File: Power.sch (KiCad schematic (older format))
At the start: 3 parts

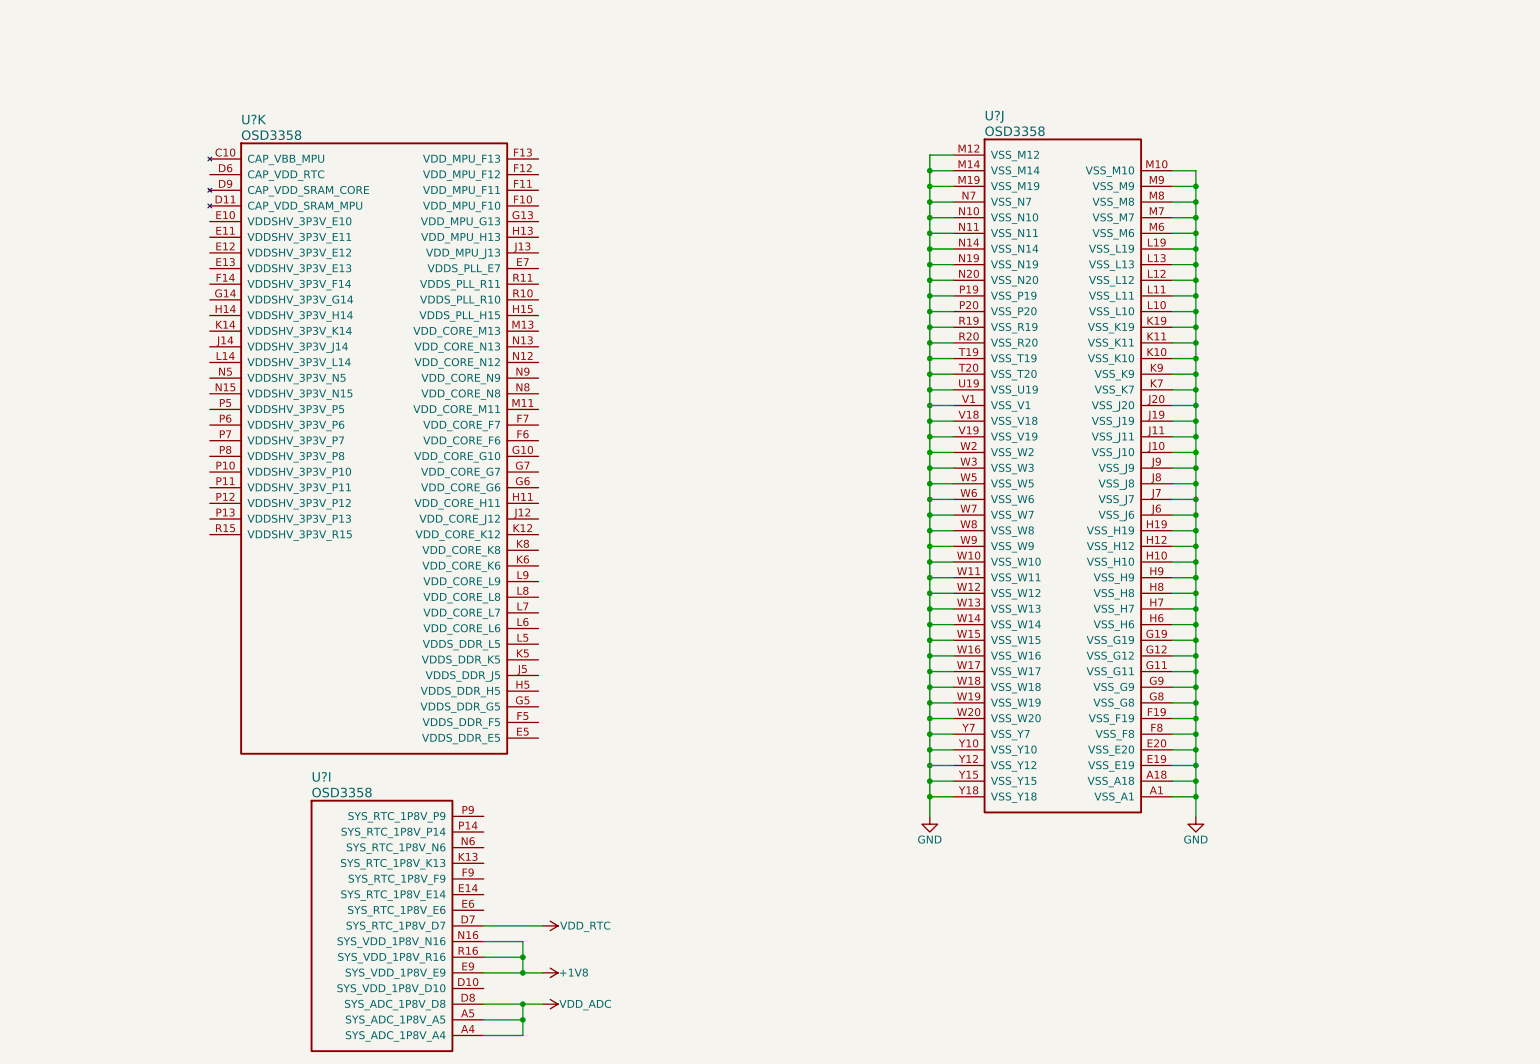
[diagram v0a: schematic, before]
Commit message: Added analog and GPIO sheet
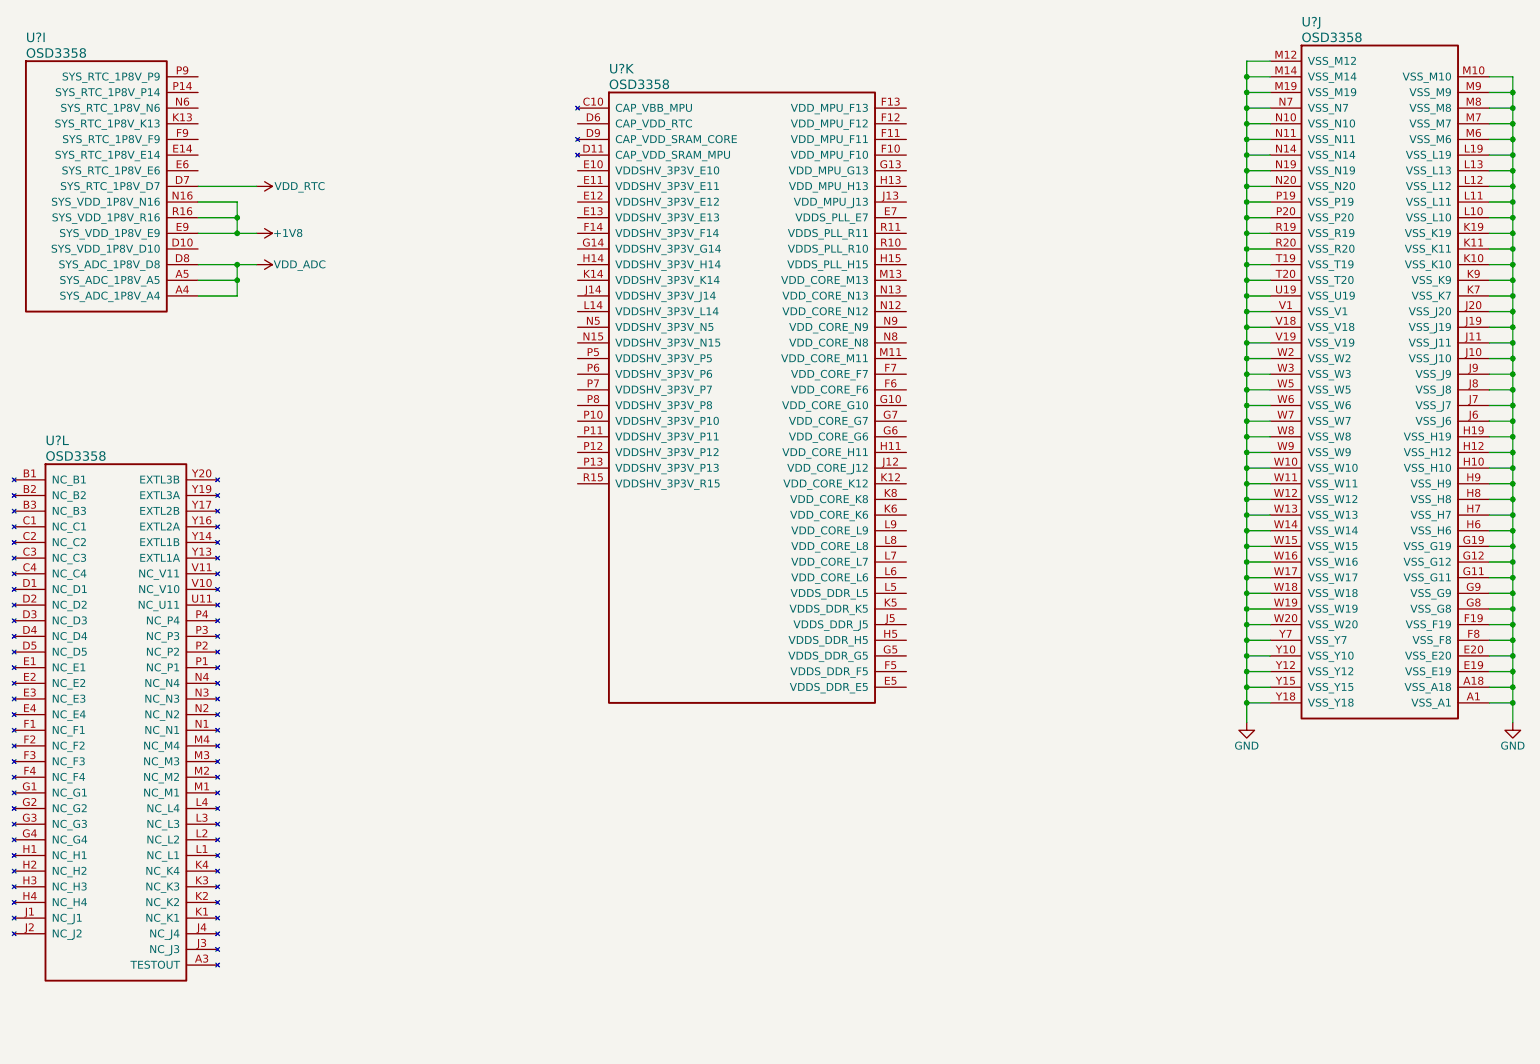
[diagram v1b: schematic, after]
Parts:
- added U?: OSD3358, symbol OSD3358
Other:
- moved on the sheet: U?I, U?J, U?K
